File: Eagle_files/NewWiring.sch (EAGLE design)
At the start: 60 parts, among them T1 PIN, T2 PIN

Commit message: Updates
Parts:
- renumbered U$11 to CA, U$12 to CB
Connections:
- net N$11: now also R10.T; no longer R10.P$3
- net N$12: now also R08.T, R09.C; no longer R08.P$3, R09.P$1
- net N$14: now also R11.R; no longer R11.P$2
- net N$15: now also R09.T, R11.C; no longer R09.P$3, R11.P$1
- net N$16: now also R09.R, R10.C; no longer R09.P$2, R10.P$1
- net N$23: now also R06.T; no longer R06.P$3
- net N$24: now also R07.T; no longer R07.P$3
- net N$25: now also R05.T; no longer R05.P$3
- net N$42: now also R02.C; no longer R02.P$1
- net N$43: now also R03.C; no longer R03.P$1
- net N$45: now also R06.C; no longer R06.P$1
- net N$47: now also R04.T; no longer R04.P$3
- net N$6: now also R01.T; no longer R01.P$3
- net N$7: now also R10.R; no longer R10.P$2
- net N$9: now also R11.T; no longer R11.P$3
- net NEUTRAL: now also R01.C, R07.C, R08.C; no longer R01.P$1, R07.P$1, R08.P$1
- net PHASE3: now also R02.T, R03.T, R04.C, R05.C; no longer R02.P$3, R03.P$3, R04.P$1, R05.P$1
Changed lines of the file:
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@@
 <part name="CI1" library="Kostas" deviceset="PIN" device=""/>
 <part name="CI2" library="Kostas" deviceset="PIN" device=""/>
-<part name="U$11" library="Kostas" deviceset="PIN" device=""/>
-<part name="U$12" library="Kostas" deviceset="PIN" device=""/>
+<part name="CA" library="Kostas" deviceset="PIN" device=""/>
+<part name="CB" library="Kostas" deviceset="PIN" device=""/>
 <part name="L3" library="Kostas" deviceset="PIN" device=""/>
 <part name="L1" library="Kostas" deviceset="PIN" device=""/>
@@
 <instance part="CI1" gate="PIN" x="170.18" y="66.04" rot="R270"/>
 <instance part="CI2" gate="PIN" x="170.18" y="45.72" rot="R90"/>
-<instance part="U$11" gate="PIN" x="228.6" y="124.46"/>
-<instance part="U$12" gate="PIN" x="246.38" y="124.46" rot="R180"/>
+<instance part="CA" gate="PIN" x="228.6" y="124.46"/>
+<instance part="CB" gate="PIN" x="246.38" y="124.46" rot="R180"/>
 <instance part="L3" gate="PIN" x="43.18" y="10.16" rot="R180"/>
 <instance part="L1" gate="PIN" x="30.48" y="22.86" rot="R270"/>
@@
 <wire x1="45.72" y1="198.12" x2="213.36" y2="198.12" width="0.3048" layer="91"/>
 <wire x1="213.36" y1="198.12" x2="233.68" y2="198.12" width="0.3048" layer="91"/>
-<pinref part="R01" gate="RELAY" pin="P$1"/>
-<pinref part="R07" gate="RELAY" pin="P$1"/>
+<pinref part="R01" gate="RELAY" pin="C"/>
+<pinref part="R07" gate="RELAY" pin="C"/>
 <wire x1="208.28" y1="185.42" x2="213.36" y2="185.42" width="0.3048" layer="91"/>
 <wire x1="213.36" y1="185.42" x2="213.36" y2="198.12" width="0.3048" layer="91"/>
 <junction x="213.36" y="198.12"/>
-<pinref part="R08" gate="RELAY" pin="P$1"/>
+<pinref part="R08" gate="RELAY" pin="C"/>
 <wire x1="233.68" y1="198.12" x2="233.68" y2="187.96" width="0.3048" layer="91"/>
 <pinref part="E7" gate="CABLE" pin="PIN1"/>
@@
 <wire x1="208.28" y1="93.98" x2="261.62" y2="81.28" width="0.3048" layer="91"/>
 <wire x1="261.62" y1="81.28" x2="261.62" y2="76.2" width="0.3048" layer="91"/>
-<pinref part="R10" gate="RELAY" pin="P$3"/>
+<pinref part="R10" gate="RELAY" pin="T"/>
 <wire x1="208.28" y1="96.52" x2="208.28" y2="93.98" width="0.1524" layer="91"/>
 <pinref part="C6" gate="CABLE" pin="PIN1"/>
@@
 <segment>
 <wire x1="213.36" y1="81.28" x2="266.7" y2="96.52" width="0.3048" layer="91"/>
-<pinref part="R11" gate="RELAY" pin="P$2"/>
+<pinref part="R11" gate="RELAY" pin="R"/>
 <pinref part="D2" gate="CABLE" pin="PIN1"/>
 <wire x1="213.36" y1="76.2" x2="213.36" y2="81.28" width="0.3048" layer="91"/>
@@
 <wire x1="238.76" y1="139.7" x2="269.24" y2="139.7" width="0.3048" layer="91"/>
 <wire x1="269.24" y1="139.7" x2="269.24" y2="124.46" width="0.3048" layer="91"/>
-<pinref part="R09" gate="RELAY" pin="P$3"/>
-<pinref part="R11" gate="RELAY" pin="P$1"/>
+<pinref part="R09" gate="RELAY" pin="T"/>
+<pinref part="R11" gate="RELAY" pin="C"/>
 <wire x1="269.24" y1="114.3" x2="269.24" y2="124.46" width="0.3048" layer="91"/>
 <pinref part="D6" gate="CABLE" pin="PIN1"/>
@@
 <wire x1="205.74" y1="139.7" x2="205.74" y2="124.46" width="0.3048" layer="91"/>
 <junction x="205.74" y="124.46"/>
-<pinref part="R09" gate="RELAY" pin="P$2"/>
+<pinref part="R09" gate="RELAY" pin="R"/>
 <wire x1="233.68" y1="139.7" x2="233.68" y2="147.32" width="0.3048" layer="91"/>
-<pinref part="R10" gate="RELAY" pin="P$1"/>
+<pinref part="R10" gate="RELAY" pin="C"/>
 <wire x1="205.74" y1="114.3" x2="205.74" y2="124.46" width="0.3048" layer="91"/>
 <pinref part="E2" gate="CABLE" pin="PIN1"/>
@@
 <wire x1="86.36" y1="119.38" x2="93.98" y2="119.38" width="0.3048" layer="91"/>
 <wire x1="93.98" y1="116.84" x2="93.98" y2="119.38" width="0.3048" layer="91"/>
-<pinref part="R04" gate="RELAY" pin="P$1"/>
-<pinref part="R05" gate="RELAY" pin="P$1"/>
+<pinref part="R04" gate="RELAY" pin="C"/>
+<pinref part="R05" gate="RELAY" pin="C"/>
 <junction x="66.04" y="119.38"/>
-<pinref part="R03" gate="RELAY" pin="P$3"/>
+<pinref part="R03" gate="RELAY" pin="T"/>
 <wire x1="86.36" y1="121.92" x2="86.36" y2="119.38" width="0.3048" layer="91"/>
 <junction x="86.36" y="119.38"/>
-<pinref part="R02" gate="RELAY" pin="P$3"/>
+<pinref part="R02" gate="RELAY" pin="T"/>
 <wire x1="66.04" y1="121.92" x2="66.04" y2="119.38" width="0.3048" layer="91"/>
 <pinref part="C1" gate="CABLE" pin="PIN1"/>
@@
 <net name="N$6" class="0">
 <segment>
-<pinref part="R01" gate="RELAY" pin="P$3"/>
+<pinref part="R01" gate="RELAY" pin="T"/>
 <pinref part="E5" gate="CABLE" pin="PIN1"/>
 <wire x1="30.48" y1="121.92" x2="30.48" y2="38.1" width="0.3048" layer="91"/>
@@
 <net name="N$7" class="0">
 <segment>
-<pinref part="R10" gate="RELAY" pin="P$2"/>
+<pinref part="R10" gate="RELAY" pin="R"/>
 <pinref part="D4" gate="CABLE" pin="PIN1"/>
 <wire x1="203.2" y1="76.2" x2="203.2" y2="96.52" width="0.3048" layer="91"/>
@@
 <net name="N$9" class="0">
 <segment>
-<pinref part="R11" gate="RELAY" pin="P$3"/>
+<pinref part="R11" gate="RELAY" pin="T"/>
 <pinref part="C2" gate="CABLE" pin="PIN1"/>
 <wire x1="271.78" y1="76.2" x2="271.78" y2="96.52" width="0.3048" layer="91"/>
@@
 <net name="N$12" class="0">
 <segment>
-<pinref part="R08" gate="RELAY" pin="P$3"/>
-<pinref part="R09" gate="RELAY" pin="P$1"/>
+<pinref part="R08" gate="RELAY" pin="T"/>
+<pinref part="R09" gate="RELAY" pin="C"/>
 <wire x1="236.22" y1="170.18" x2="236.22" y2="165.1" width="0.3048" layer="91"/>
 </segment>
@@
 <segment>
 <pinref part="D6" gate="CABLE" pin="PIN2"/>
-<pinref part="U$12" gate="PIN" pin="PIN1"/>
+<pinref part="CB" gate="PIN" pin="PIN1"/>
 <wire x1="246.38" y1="124.46" x2="251.46" y2="124.46" width="0.1524" layer="91"/>
 </segment>
@@
 <net name="N$33" class="1">
 <segment>
-<pinref part="U$11" gate="PIN" pin="PIN1"/>
+<pinref part="CA" gate="PIN" pin="PIN1"/>
 <wire x1="220.98" y1="124.46" x2="228.6" y2="124.46" width="0.1524" layer="91"/>
 <pinref part="E2" gate="CABLE" pin="PIN2"/>
@@
 <net name="N$42" class="0">
 <segment>
-<pinref part="R02" gate="RELAY" pin="P$1"/>
+<pinref part="R02" gate="RELAY" pin="C"/>
 <pinref part="C8" gate="CABLE" pin="PIN1"/>
 <wire x1="63.5" y1="142.24" x2="63.5" y2="139.7" width="0.3048" layer="91"/>
@@
 <segment>
 <pinref part="C7" gate="CABLE" pin="PIN1"/>
-<pinref part="R03" gate="RELAY" pin="P$1"/>
+<pinref part="R03" gate="RELAY" pin="C"/>
 <wire x1="83.82" y1="139.7" x2="83.82" y2="142.24" width="0.3048" layer="91"/>
 </segment>
@@
 <net name="N$45" class="0">
 <segment>
-<pinref part="R06" gate="RELAY" pin="P$1"/>
+<pinref part="R06" gate="RELAY" pin="C"/>
 <pinref part="D11" gate="CABLE" pin="PIN1"/>
 <wire x1="134.62" y1="142.24" x2="134.62" y2="121.92" width="0.3048" layer="91"/>
@@
 <net name="N$47" class="0">
 <segment>
-<pinref part="R04" gate="RELAY" pin="P$3"/>
+<pinref part="R04" gate="RELAY" pin="T"/>
 <wire x1="68.58" y1="99.06" x2="68.58" y2="88.9" width="0.3048" layer="91"/>
 <pinref part="E4" gate="CABLE" pin="PIN1"/>
@@
 <segment>
 <pinref part="D3" gate="CABLE" pin="PIN1"/>
-<pinref part="R05" gate="RELAY" pin="P$3"/>
+<pinref part="R05" gate="RELAY" pin="T"/>
 <wire x1="96.52" y1="99.06" x2="96.52" y2="88.9" width="0.3048" layer="91"/>
 </segment>
@@
 <net name="N$23" class="0">
 <segment>
-<pinref part="R06" gate="RELAY" pin="P$3"/>
+<pinref part="R06" gate="RELAY" pin="T"/>
 <wire x1="137.16" y1="104.14" x2="137.16" y2="99.06" width="0.3048" layer="91"/>
 <pinref part="C12" gate="CABLE" pin="PIN1"/>
@@
 <net name="N$24" class="0">
 <segment>
-<pinref part="R07" gate="RELAY" pin="P$3"/>
+<pinref part="R07" gate="RELAY" pin="T"/>
 <wire x1="190.5" y1="182.88" x2="185.42" y2="182.88" width="0.3048" layer="91"/>
 <pinref part="C11" gate="CABLE" pin="PIN1"/>

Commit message: Modified
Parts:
- added N1: CABLE, Kostas:CABLE
- added R12, R13, R14, R15, R16: RELAY, Kostas:RELAY
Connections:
- new net N$5: B6.PIN1, B7.PIN1, N1.PIN1
- net D10: no longer HOT_WATER_VALVE.P$1
- net N$13: now also HOT_WATER_VALVE.P$1, N1.PIN2; no longer B6.PIN1, B7.PIN1
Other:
- note added: "NOT USED"
- moved on the sheet: COLD_WATER_VALVE, HOT_WATER_VALVE
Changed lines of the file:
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@@
 <part name="E4" library="Kostas" deviceset="CABLE" device=""/>
 <part name="E6" library="Kostas" deviceset="CABLE" device=""/>
+<part name="R12" library="Kostas" deviceset="RELAY" device=""/>
+<part name="R13" library="Kostas" deviceset="RELAY" device=""/>
+<part name="R14" library="Kostas" deviceset="RELAY" device=""/>
+<part name="R15" library="Kostas" deviceset="RELAY" device=""/>
+<part name="R16" library="Kostas" deviceset="RELAY" device=""/>
+<part name="N1" library="Kostas" deviceset="CABLE" device=""/>
 </parts>
 <sheets>
@@
 <text x="198.12" y="55.88" size="1.778" layer="97" rot="R90" align="center">WASH MOTOR</text>
 <text x="160.02" y="55.88" size="1.778" layer="97" rot="R90" align="center">PUMP</text>
+<text x="302.26" y="195.58" size="3.048" layer="95" align="center">NOT USED</text>
 </plain>
 <instances>
@@
 <instance part="L2" gate="PIN" x="27.94" y="10.16"/>
 <instance part="E5" gate="CABLE" x="30.48" y="38.1" rot="R270"/>
-<instance part="COLD_WATER_VALVE" gate="VALVE" x="71.12" y="58.42" rot="R90"/>
-<instance part="HOT_WATER_VALVE" gate="VALVE" x="99.06" y="58.42" rot="R90"/>
+<instance part="COLD_WATER_VALVE" gate="VALVE" x="71.12" y="66.04" rot="R90"/>
+<instance part="HOT_WATER_VALVE" gate="VALVE" x="99.06" y="66.04" rot="R90"/>
 <instance part="R04" gate="RELAY" x="66.04" y="114.3" rot="MR270"/>
 <instance part="R05" gate="RELAY" x="93.98" y="114.3" rot="MR270"/>
@@
 <instance part="E4" gate="CABLE" x="68.58" y="88.9" rot="R270"/>
 <instance part="E6" gate="CABLE" x="22.86" y="198.12" rot="R180"/>
+<instance part="R12" gate="RELAY" x="307.34" y="182.88" rot="MR0"/>
+<instance part="R13" gate="RELAY" x="307.34" y="167.64" rot="MR0"/>
+<instance part="R14" gate="RELAY" x="307.34" y="152.4" rot="MR0"/>
+<instance part="R15" gate="RELAY" x="307.34" y="137.16" rot="MR0"/>
+<instance part="R16" gate="RELAY" x="307.34" y="121.92" rot="MR0"/>
+<instance part="N1" gate="CABLE" x="116.84" y="53.34" rot="R180"/>
 </instances>
 <busses>
@@
 <pinref part="COLD_WATER_VALVE" gate="VALVE" pin="P$2"/>
 <pinref part="E4" gate="CABLE" pin="PIN2"/>
-<wire x1="68.58" y1="81.28" x2="68.58" y2="68.58" width="0.1524" layer="91"/>
+<wire x1="68.58" y1="81.28" x2="68.58" y2="76.2" width="0.1524" layer="91"/>
 </segment>
 </net>
@@
 <segment>
 <pinref part="HOT_WATER_VALVE" gate="VALVE" pin="P$2"/>
-<wire x1="96.52" y1="68.58" x2="96.52" y2="81.28" width="0.1524" layer="91"/>
+<wire x1="96.52" y1="76.2" x2="96.52" y2="81.28" width="0.1524" layer="91"/>
 <pinref part="D3" gate="CABLE" pin="PIN2"/>
 </segment>
@@
 <segment>
 <pinref part="COLD_WATER_VALVE" gate="VALVE" pin="P$1"/>
-<wire x1="71.12" y1="58.42" x2="71.12" y2="45.72" width="0.1524" layer="91"/>
 <pinref part="D10" gate="CABLE" pin="PIN2"/>
-<pinref part="HOT_WATER_VALVE" gate="VALVE" pin="P$1"/>
-<wire x1="71.12" y1="45.72" x2="71.12" y2="22.86" width="0.1524" layer="91"/>
-<wire x1="99.06" y1="58.42" x2="99.06" y2="45.72" width="0.1524" layer="91"/>
-<wire x1="71.12" y1="45.72" x2="99.06" y2="45.72" width="0.1524" layer="91"/>
-<junction x="71.12" y="45.72"/>
+<wire x1="71.12" y1="66.04" x2="71.12" y2="22.86" width="0.1524" layer="91"/>
 </segment>
 </net>
@@
 </segment>
 </net>
-<net name="N$13" class="0">
-<segment>
-<pinref part="B6" gate="CABLE" pin="PIN1"/>
-<pinref part="B7" gate="CABLE" pin="PIN1"/>
-<wire x1="137.16" y1="55.88" x2="137.16" y2="50.8" width="0.3048" layer="91"/>
-</segment>
-</net>
 <net name="N$23" class="0">
 <segment>
@@
 </segment>
 </net>
+<net name="N$5" class="0">
+<segment>
+<pinref part="B6" gate="CABLE" pin="PIN1"/>
+<pinref part="B7" gate="CABLE" pin="PIN1"/>
+<wire x1="116.84" y1="53.34" x2="137.16" y2="53.34" width="0.3048" layer="91"/>
+<wire x1="137.16" y1="55.88" x2="137.16" y2="53.34" width="0.3048" layer="91"/>
+<wire x1="137.16" y1="53.34" x2="137.16" y2="50.8" width="0.3048" layer="91"/>
+<junction x="137.16" y="53.34"/>
+<pinref part="N1" gate="CABLE" pin="PIN1"/>
+</segment>
+</net>
+<net name="N$13" class="0">
+<segment>
+<pinref part="N1" gate="CABLE" pin="PIN2"/>
+<pinref part="HOT_WATER_VALVE" gate="VALVE" pin="P$1"/>
+<wire x1="99.06" y1="66.04" x2="99.06" y2="53.34" width="0.1524" layer="91"/>
+<wire x1="99.06" y1="53.34" x2="109.22" y2="53.34" width="0.1524" layer="91"/>
+</segment>
+</net>

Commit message: Update
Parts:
- removed .S1, .S2, CA, CB, CI1, CI2, L1, L2, L3, MC1, MC2, MCC, MP1, MP2, MPC, S1, S2, T1, T2: PIN, Kostas:PIN
- removed H1, H2: PIN, Connectors:PIN
- added CAPACITOR: CAPACITOR, Kostas:CAPACITOR
- added HEATER: HEATER, Kostas:HEATER
- added MAIN_SWITCH: SWITCH, Kostas:SWITCH
- added PUMP: CI, Kostas:MOTOR-2
- added SPIN_MOTOR: MC, Kostas:MOTOR-3
- added THERMOSTAT: THERMOSTAT, Kostas:THERMOSTAT
- added U$1: LOCK, Kostas:LOCK
- added WASH_MOTOR: MP, Kostas:MOTOR-3
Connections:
- removed net B7: B7.PIN2, T1.PIN1
- removed net C2: C2.PIN2, MC2.PIN1
- removed net C6: C6.PIN2, MC1.PIN1
- removed net N$27: B6.PIN2, H2.PIN1
- new net N$19: C6.PIN2, SPIN_MOTOR.M1
- new net N$26: C2.PIN2, SPIN_MOTOR.M2
- new net N$28: B7.PIN2, THERMOSTAT.P$1
- new net N$29: B6.PIN2, HEATER.P$1
- net C10: now also SPIN_MOTOR.MC, WASH_MOTOR.MC; no longer MCC.PIN1, MPC.PIN1
- net C11-OVERFLOW: now also PUMP.M1; no longer CI1.PIN1
- net D2: now also WASH_MOTOR.M2; no longer MP2.PIN1
- net D4: now also WASH_MOTOR.M1; no longer MP1.PIN1
- net D6: now also CAPACITOR.C2; no longer CB.PIN1
- net E11: now also PUMP.M2; no longer CI2.PIN1
- net E5: now also U$1.N; no longer L1.PIN1
- net N$1: now also MAIN_SWITCH.OUT1; no longer .S1.PIN1
- net N$10: now also MAIN_SWITCH.IN2; no longer S2.PIN1
- net N$20: now also U$1.C; no longer L3.PIN1
- net N$21: now also HEATER.P$2; no longer H1.PIN1
- net N$22: now also THERMOSTAT.P$2; no longer T2.PIN1
- net N$3: now also MAIN_SWITCH.OUT2, U$1.L; no longer .S2.PIN1, L2.PIN1
- net N$33: now also CAPACITOR.C1; no longer CA.PIN1
- net N$8: now also MAIN_SWITCH.IN1; no longer S1.PIN1
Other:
- note removed: "C"
- note removed: "CAPACITOR"
- note removed: "CI"
- note removed: "HEATER"
- note removed: "L"
- note removed: "MC"
- note removed: "MP"
- note removed: "N"
- note removed: "PUMP"
- note removed: "SPIN MOTOR"
- note removed: "THERMOSTAT"
- note removed: "WASH MOTOR"
- moved on the sheet: B7, C11, C12, D3, D6, E11, E12, E2, E4, N1, R06, R07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

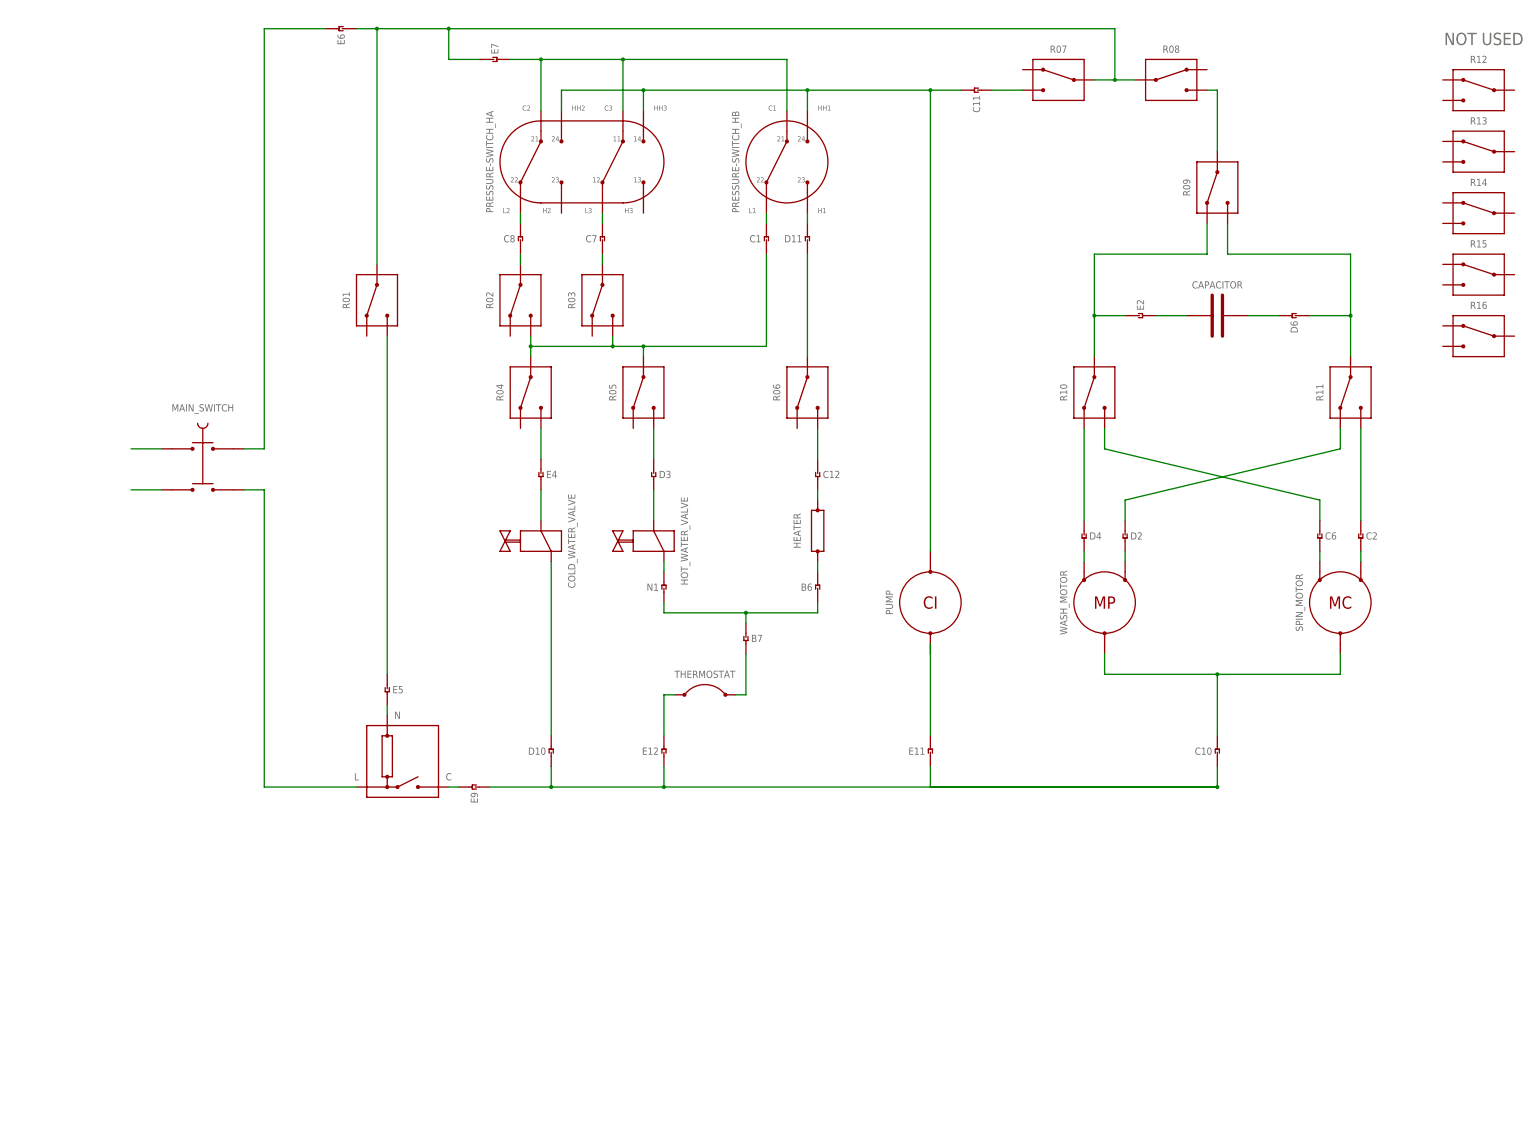
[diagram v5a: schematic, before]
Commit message: Added Cabling
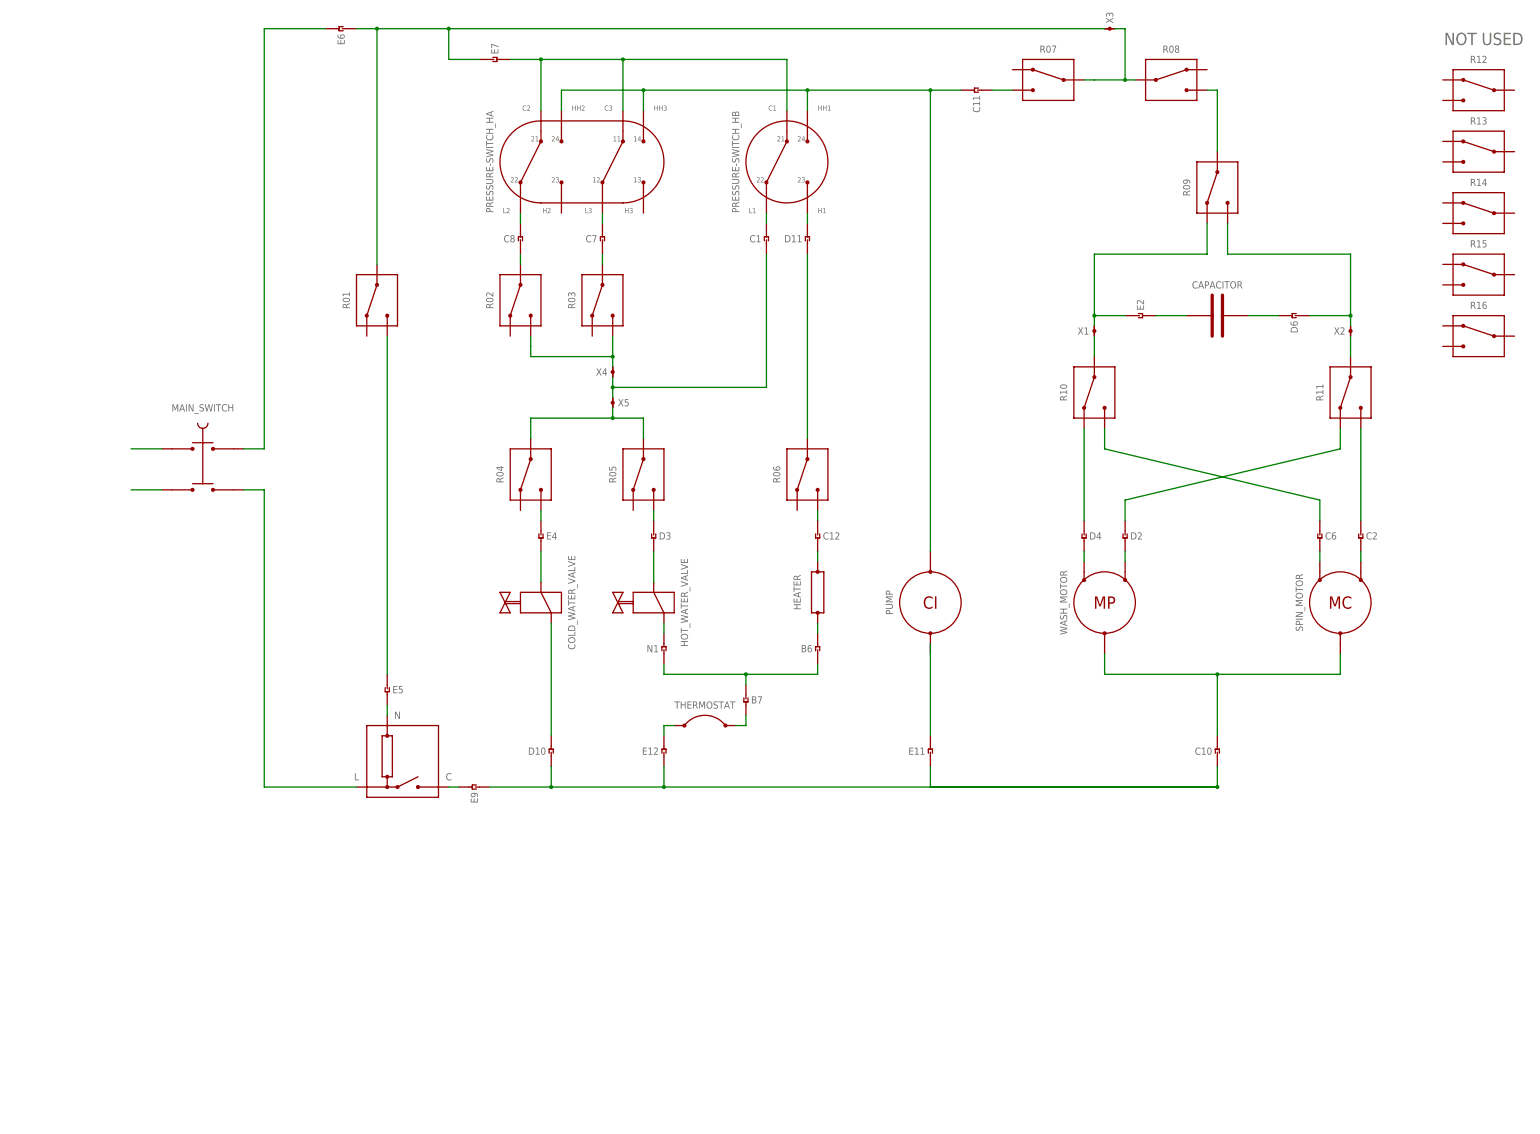
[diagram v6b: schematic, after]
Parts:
- added X1, X2, X3, X4, X5: DOMINO, Kostas:DOMINO
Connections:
- new net N$27: E2.PIN1, R09.R, X1.PIN2
- new net N$30: D6.PIN1, R09.T, X2.PIN2
- new net N$31: R11.C, X2.PIN1
- new net N$32: R07.C, R08.C, X3.PIN2
- new net N$35: R04.C, R05.C, X5.PIN2
- net N$15: now also R10.C, X1.PIN1; no longer D6.PIN1, R09.T, R11.C
- net N$16: now also R02.T, R03.T, X4.PIN2; no longer E2.PIN1, R09.R, R10.C
- net NEUTRAL: now also X3.PIN1; no longer R07.C, R08.C
- net PHASE3: now also X4.PIN1, X5.PIN1; no longer R02.T, R03.T, R04.C, R05.C
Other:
- moved on the sheet: B6, B7, C12, COLD_WATER_VALVE, D3, E4, HEATER, HOT_WATER_VALVE, N1, R04, R05, R06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
